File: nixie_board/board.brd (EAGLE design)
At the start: 250 x 100 mm, 44 parts, among them IC1 74141N, IC2 74HC138D, IC3 74HC138D, U1 ATMEGA328P-AU

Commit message: [add]iroiro
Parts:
- removed U1: ATMEGA328P-AU, Atmel-ATMEGA328P-AU:QFP80P900X900X120-32N
- added C2, C3: (no value), 160713 Library by matsu:E2,5-6
- added IC4: LT1963ES8-3.3, linear-technology:SOIC8
- added IC5: FT232RL, ftdichip:SSOP28
- added U$4: DC_JACK_2DC0005D100, 160713 Library by matsu:DC_JACK_2DC0005D100
- added U2: ESP-WROOM-32, esp32:ESP-WROOM-32
- U$2: value FA-238 -> PIN_HEADER_MALE_1X08_08P; device crystals:FA-238 -> 160713 Library by matsu:PIN_HEADER_MALE_1X08_08P
- moved U$2 96.2 mm to (42.0, 4.00), turned to 0 degrees
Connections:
- new net +3V3: C2.+, IC1.5, IC2.16, IC4.1, IC4.2, R10.2, U2.2
- new net N$16: U2.3
- new net VCCIO: IC5.4
- net +5V: now also C3.+, IC4.5, IC4.8; no longer IC1.5, IC2.16, IC2.6, R10.2, U1.18, U1.4, U1.6
- net GND: now also C2.-, C3.-, IC4.3, IC4.6, IC4.7, IC5.18, IC5.21, IC5.25, IC5.7, U2.1, U2.15, U2.38, U2.GND; no longer U$2.2, U$2.4, U1.21, U1.3, U1.5
- net LHDP: no longer U1.1
- net N$1: now also IC2.6; no longer U$2.3, U1.7
- net N$15: no longer U1.29
- net N$2: now also IC3.16; no longer U$2.1, U1.8
- net N$3: now also U2.13; no longer U1.11
- net N$4: now also U2.12; no longer U1.10
- net N$5: now also U2.11; no longer U1.9
- net N$6: now also U2.10; no longer U1.2
- net NIX1: now also U2.9; no longer U1.26
- net NIX2: now also U2.8; no longer U1.25
- net NIX3: now also U2.7; no longer U1.24
- net NIX4: now also U2.6; no longer U1.23
- net RHDP: no longer U1.32
- net RXI: no longer U1.30
- net TXO: no longer U1.31
- net VCC: now also IC5.20; no longer IC3.16

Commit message: [add]complete
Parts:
- removed C1: (no value), 160713 Library by matsu:E5-8,5
- removed C2, C3: (no value), 160713 Library by matsu:E2,5-6
- removed IC1: 74141N, 74xx-eu:DIL16
- removed IC2, IC3: 74HC138D, 74xx-eu:SO16
- removed IC4: LT1963ES8-3.3, linear-technology:SOIC8
- removed IC5: FT232RL, ftdichip:SSOP28
- removed N10: IN-19B, russian-nixies:IN-19
- removed N9: IN-19A, russian-nixies:IN-19
- removed R1, R17, R18, R19, R2, R20, R21, R22, R23, R24, R25, R26, R27, R28, R29, R3, R30, R4, R5, R6, R7, R8: (no value), resistor:M3216
- removed R10: (no value), 160713 Library by matsu:R3216
- removed RESET: DTS-6, 160713 Library by matsu:DTS6
- removed U$3, U$5, U$6: TLP627-4, 160713 Library by matsu:TLP627-4
- removed U$4: DC_JACK_2DC0005D100, 160713 Library by matsu:DC_JACK_2DC0005D100
- removed U2: ESP-WROOM-32, esp32:ESP-WROOM-32
- added LED1, LED2, LED3, LED4, LED5, LED6, LED7, LED8: WS2812B_5050N, adafruit:WS2812B-NARROW
- U$1: value MICRO-USB-ZX62R-B-5P -> PIN_HEADER_MALE_2X10_20P; device con-hirose:ZX62R-B-5P -> 160713 Library by matsu:PIN_HEADER_MALE_2X10_20P
- U$2: value PIN_HEADER_MALE_1X08_08P -> PIN_HEADER_MALE_1X03_03P; device 160713 Library by matsu:PIN_HEADER_MALE_1X08_08P -> 160713 Library by matsu:PIN_HEADER_MALE_1X03_03P
- moved U$1 109.2 mm to (120.0, 39.0), turned to 0 degrees
- moved U$2 66.9 mm to (99.0, 39.0)
- moved N1 29.1 mm to (21.0, 21.0)
- moved N2 29.1 mm to (48.5, 21.0)
- moved N3 29.1 mm to (77.0, 21.0)
- moved N4 29.1 mm to (105.5, 21.0)
- moved N5 29.1 mm to (134.0, 21.0)
- moved N6 29.1 mm to (162.5, 21.0)
- moved N7 29.1 mm to (191.0, 21.0)
- moved N8 29.1 mm to (219.5, 21.0)
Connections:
- removed net +3V3: C2.+, IC1.5, IC2.16, IC4.1, IC4.2, R10.2, U2.2
- removed net 200V: R21.2, R22.2, R23.2, R24.2, R29.2, R30.2, R5.2, R6.2, R7.2, R8.2
- removed net ANODE0: IC2.15, U$3.P$2
- removed net ANODE1: IC2.14, U$3.P$4
- removed net ANODE10: IC3.13
- removed net ANODE11: IC3.12
- removed net ANODE12: IC3.11
- removed net ANODE13: IC3.10
- removed net ANODE14: IC3.9
- removed net ANODE15: IC3.7
- removed net ANODE2: IC2.13, U$3.P$6
- removed net ANODE3: IC2.12, U$3.P$8
- removed net ANODE4: IC2.10, U$5.P$2
- removed net ANODE5: IC2.11, U$5.P$4
- removed net ANODE6: IC2.9, U$5.P$6
- removed net ANODE7: IC2.7, U$5.P$8
- removed net ANODE8: IC3.15, U$6.P$2
- removed net ANODE9: IC3.14, U$6.P$4
- removed net DTR: U$1.1
- removed net LHDP: U$6.P$6
- removed net N$10: R4.2, U$3.P$7
- removed net N$11: R8.1, U$3.P$10
- removed net N$12: R7.1, U$3.P$12
- removed net N$13: R6.1, U$3.P$14
- removed net N$14: R5.1, U$3.P$16
- removed net N$15: R10.1, RESET.3, RESET.4
- removed net N$16: U2.3
- removed net N$23: R17.2, U$5.P$1
- removed net N$24: R18.2, U$5.P$3
- removed net N$25: R19.2, U$5.P$5
- removed net N$26: R20.2, U$5.P$7
- removed net N$27: R24.1, U$5.P$10
- removed net N$28: R23.1, U$5.P$12
- removed net N$29: R22.1, U$5.P$14
- removed net N$30: R21.1, U$5.P$16
- removed net N$31: R25.2, U$6.P$1
- removed net N$32: R26.2, U$6.P$3
- removed net N$33: R27.2, U$6.P$5
- removed net N$34: R28.2, U$6.P$7
- removed net N$37: R30.1, U$6.P$14
- removed net N$38: R29.1, U$6.P$16
- removed net N$9: R3.2, U$3.P$5
- removed net NIX1: IC2.1, IC3.1, U2.9
- removed net NIX2: IC2.2, IC3.2, U2.8
- removed net NIX3: IC2.3, IC3.3, U2.7
- removed net NIX4: IC2.4, IC3.6, U2.6
- removed net NIXIE_ANODE10: N10.8, U$6.P$13
- removed net NIXIE_ANODE9: N9.8, U$6.P$15
- removed net RHDP: U$6.P$8
- removed net RXI: U$1.3
- removed net TXO: U$1.2
- removed net VCC: IC5.20
- removed net VCCIO: IC5.4
- net +5V: now also LED1.1-VDD, LED2.1-VDD, LED3.1-VDD, LED4.1-VDD, LED5.1-VDD, LED6.1-VDD, LED7.1-VDD, LED8.1-VDD, U$2.P$1; no longer C1.+, C3.+, IC4.5, IC4.8, R1.1, R17.1, R18.1, R19.1, R2.1, R20.1, R25.1, R26.1, R27.1, R28.1, R3.1, R4.1, U$1.4
- net DOT0: now also U$1.P$3; no longer U$6.P$12
- net DOT1: now also U$1.P$1; no longer U$6.P$10
- net GND: now also LED1.3-GND, LED2.3-GND, LED3.3-GND, LED4.3-GND, LED5.3-GND, LED6.3-GND, LED7.3-GND, LED8.3-GND, U$2.P$2; no longer C1.-, C2.-, C3.-, IC1.12, IC2.5, IC2.8, IC3.4, IC3.5, IC3.8, IC4.3, IC4.6, IC4.7, IC5.18, IC5.21, IC5.25, IC5.7, RESET.1, RESET.2, U$1.5, U$6.P$11, U$6.P$9, U2.1, U2.15, U2.38, U2.GND
- net N$1: now also LED1.2-DOUT, LED2.4-DIN; no longer IC2.6
- net N$2: now also LED2.2-DOUT, LED3.4-DIN; no longer IC3.16
- net N$3: now also LED3.2-DOUT, LED4.4-DIN; no longer IC1.3, U2.13
- net N$4: now also LED4.2-DOUT, LED5.4-DIN; no longer IC1.6, U2.12
- net N$5: now also LED5.2-DOUT, LED6.4-DIN; no longer IC1.7, U2.11
- net N$6: now also LED6.2-DOUT, LED7.4-DIN; no longer IC1.4, U2.10
- net N$7: now also LED7.2-DOUT, LED8.4-DIN; no longer R1.2, U$3.P$1
- net N$8: now also LED1.4-DIN, U$2.P$3; no longer R2.2, U$3.P$3
- net NIXIE0: now also U$1.P$20; no longer IC1.16, N10.5, N9.11
- net NIXIE1: now also U$1.P$18; no longer N10.11, N9.10
- net NIXIE2: now also U$1.P$16; no longer IC1.15, IC1.8, N10.12, N9.12
- net NIXIE3: now also U$1.P$14; no longer IC1.9, N10.14, N9.14
- net NIXIE4: now also U$1.P$12; no longer IC1.13, N10.2, N9.2
- net NIXIE5: now also U$1.P$10; no longer IC1.14, N10.4, N9.4
- net NIXIE6: now also U$1.P$8; no longer IC1.11, N10.10, N9.5
- net NIXIE7: now also U$1.P$6; no longer IC1.10, N10.6, N9.6
- net NIXIE8: now also U$1.P$4; no longer IC1.1
- net NIXIE9: now also U$1.P$2; no longer IC1.2
- net NIXIE_ANODE1: now also U$1.P$5; no longer U$3.P$15
- net NIXIE_ANODE2: now also U$1.P$7; no longer U$3.P$13
- net NIXIE_ANODE3: now also U$1.P$9; no longer U$3.P$11
- net NIXIE_ANODE4: now also U$1.P$11; no longer U$3.P$9
- net NIXIE_ANODE5: now also U$1.P$13; no longer U$5.P$15
- net NIXIE_ANODE6: now also U$1.P$15; no longer U$5.P$13
- net NIXIE_ANODE7: now also U$1.P$17; no longer U$5.P$11
- net NIXIE_ANODE8: now also U$1.P$19; no longer U$5.P$9
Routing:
- net NIXIE7: track 0.00 -> 263.7 mm, vias 0 -> 1
- net NIXIE9: track 0.00 -> 263.5 mm, vias 0 -> 2
- net GND: track 0.00 -> 253.3 mm, vias 0 -> 8
- net NIXIE1: track 0.00 -> 244.6 mm
- net NIXIE0: track 0.00 -> 238.5 mm
- net +5V: track 47.1 -> 284.3 mm, vias 0 -> 11
- net NIXIE5: track 0.00 -> 236.8 mm, vias 0 -> 1
- net NIXIE8: track 0.00 -> 235.7 mm, vias 0 -> 2
- net DOT0: track 0.00 -> 235.6 mm, vias 0 -> 2
- net NIXIE6: track 0.00 -> 235.1 mm, vias 0 -> 2
- net NIXIE4: track 0.00 -> 232.4 mm, vias 0 -> 1
- net NIXIE3: track 0.00 -> 230.7 mm, vias 0 -> 2
- net DOT1: track 0.00 -> 228.2 mm, vias 0 -> 3
- net NIXIE2: track 0.00 -> 221.7 mm, vias 0 -> 1
- net NIXIE_ANODE1: track 0.00 -> 108.6 mm
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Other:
- board size 250 x 100 mm -> 240 x 50 mm

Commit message: [fix] hole
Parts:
- moved LED1 1.00 mm to (20.0, 21.0)
- moved N1 1.00 mm to (20.0, 21.0)
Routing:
- net NIXIE9: track 263.5 -> 265.5 mm
- net NIXIE_ANODE1: track 108.6 -> 109.6 mm
- net NIXIE8: track 235.7 -> 236.7 mm
- net NIXIE7: track 263.7 -> 264.7 mm
- net NIXIE6: track 235.1 -> 236.1 mm
- net NIXIE5: track 236.8 -> 237.8 mm
- net NIXIE4: track 232.4 -> 233.4 mm
- net NIXIE3: track 230.7 -> 231.7 mm
- net NIXIE2: track 221.7 -> 222.7 mm
- net NIXIE1: track 244.6 -> 245.6 mm
- net NIXIE0: track 238.5 -> 239.5 mm
- net N$8: track 103.6 -> 104.6 mm
- net N$1: track 24.3 -> 25.3 mm
- net GND: track 253.3 -> 254.3 mm
- net DOT1: track 228.2 -> 229.2 mm
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
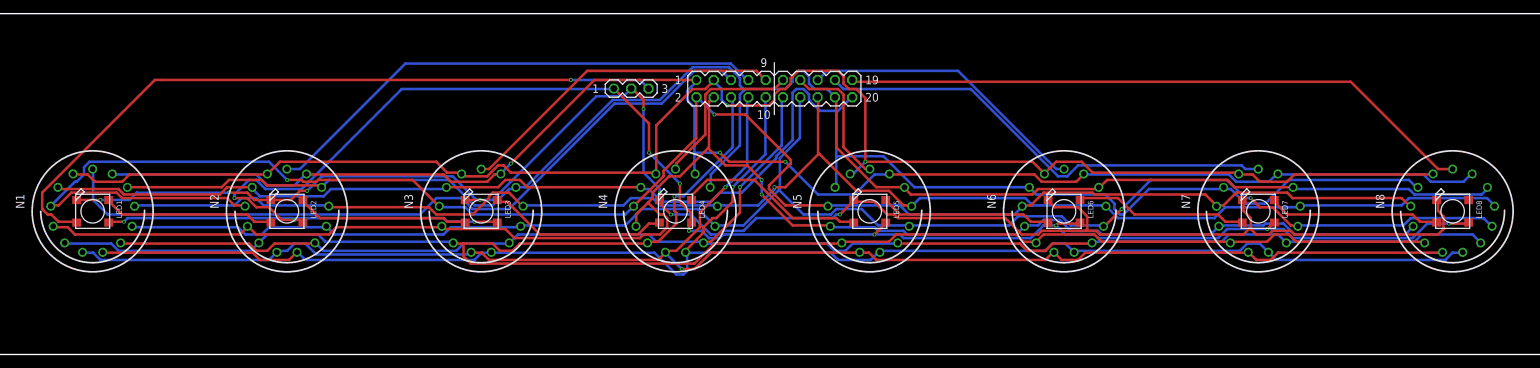
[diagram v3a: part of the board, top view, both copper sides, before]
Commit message: [fix] 太さ・ガーバー出力(FusionPCB)
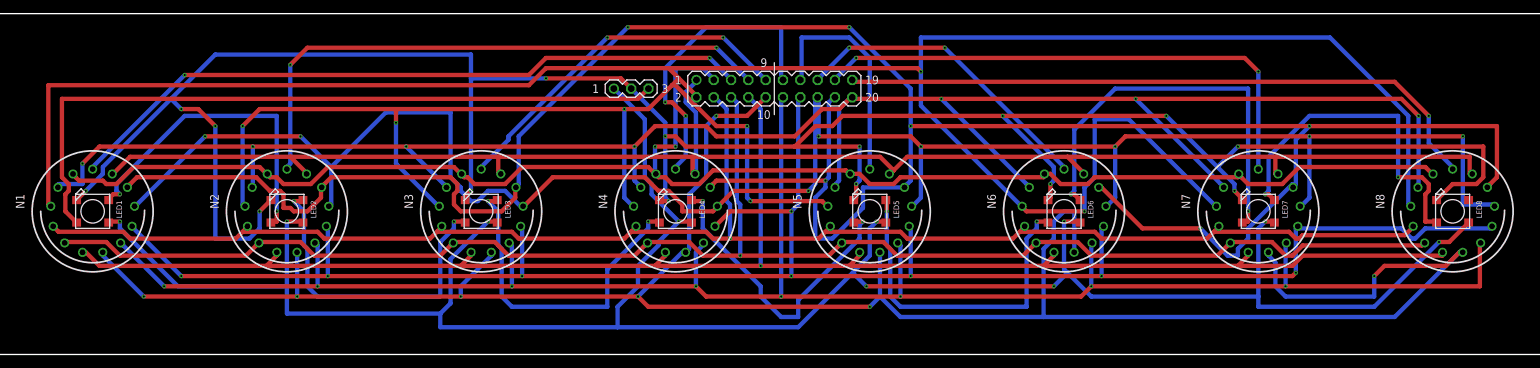
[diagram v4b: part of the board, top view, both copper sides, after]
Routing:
- net NIXIE9: track 265.5 -> 467.4 mm, vias 2 -> 7
- net NIXIE1: track 245.6 -> 362.7 mm, vias 0 -> 6
- net GND: track 254.3 -> 349.4 mm, vias 8 -> 15
- net NIXIE5: track 237.8 -> 332.4 mm, vias 1 -> 7
- net NIXIE2: track 222.7 -> 293.1 mm, vias 1 -> 8
- net NIXIE0: track 239.5 -> 291.6 mm, vias 0 -> 7
- net NIXIE3: track 231.7 -> 279.4 mm, vias 2 -> 8
- net NIXIE4: track 233.4 -> 279.7 mm, vias 1 -> 8
- net +5V: track 285.3 -> 330.6 mm, vias 11 -> 10
- net N$6: track 25.4 -> 59.8 mm, vias 0 -> 2
- net NIXIE7: track 264.7 -> 234.9 mm
- net N$7: track 25.3 -> 50.2 mm, vias 0 -> 2
- net N$5: track 25.2 -> 49.9 mm, vias 0 -> 2
- net N$2: track 25.2 -> 48.4 mm, vias 0 -> 2
- net N$1: track 25.3 -> 47.8 mm, vias 0 -> 2
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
